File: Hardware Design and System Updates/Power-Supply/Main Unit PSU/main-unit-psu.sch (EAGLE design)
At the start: 15 parts, among them U1 BA033CC0FP-E2TO252-3_ROM, U2 BA033CC0FP-E2TO252-3_ROM

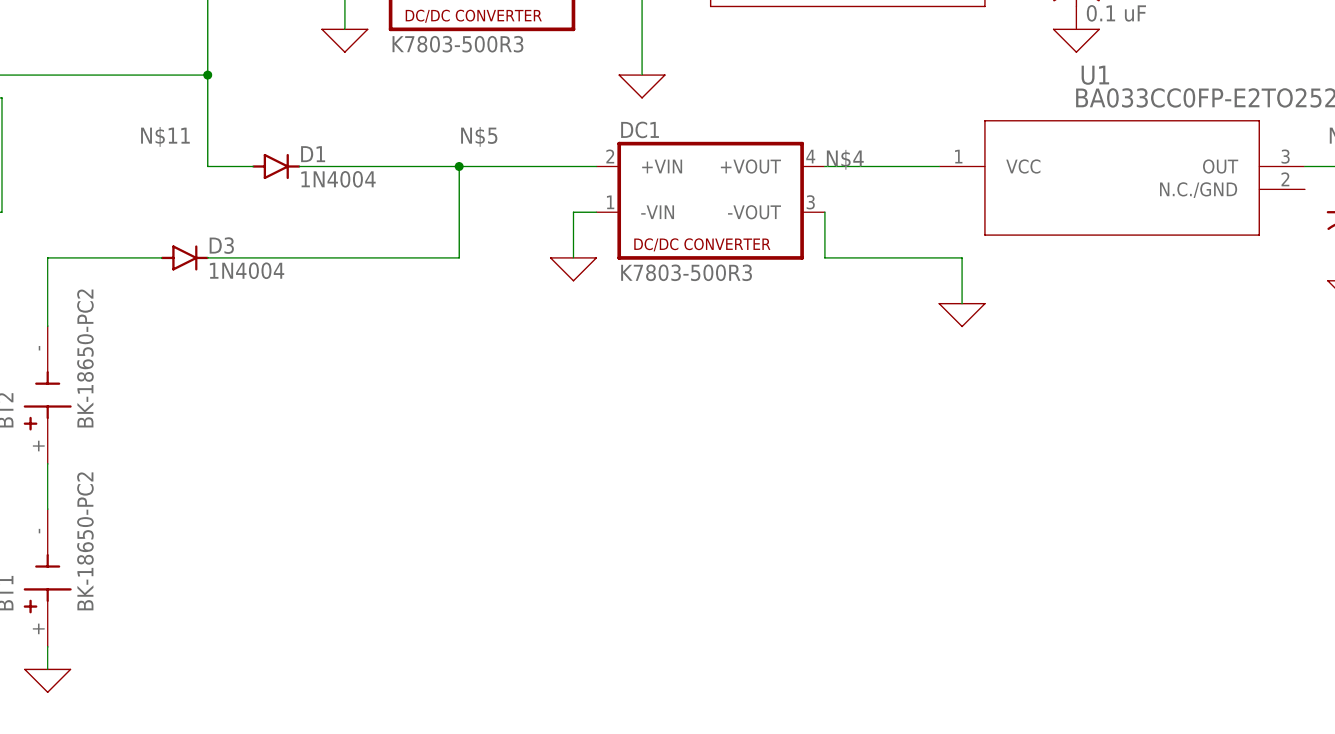
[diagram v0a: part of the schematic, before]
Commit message: Added 5V regulator to PSU schematics
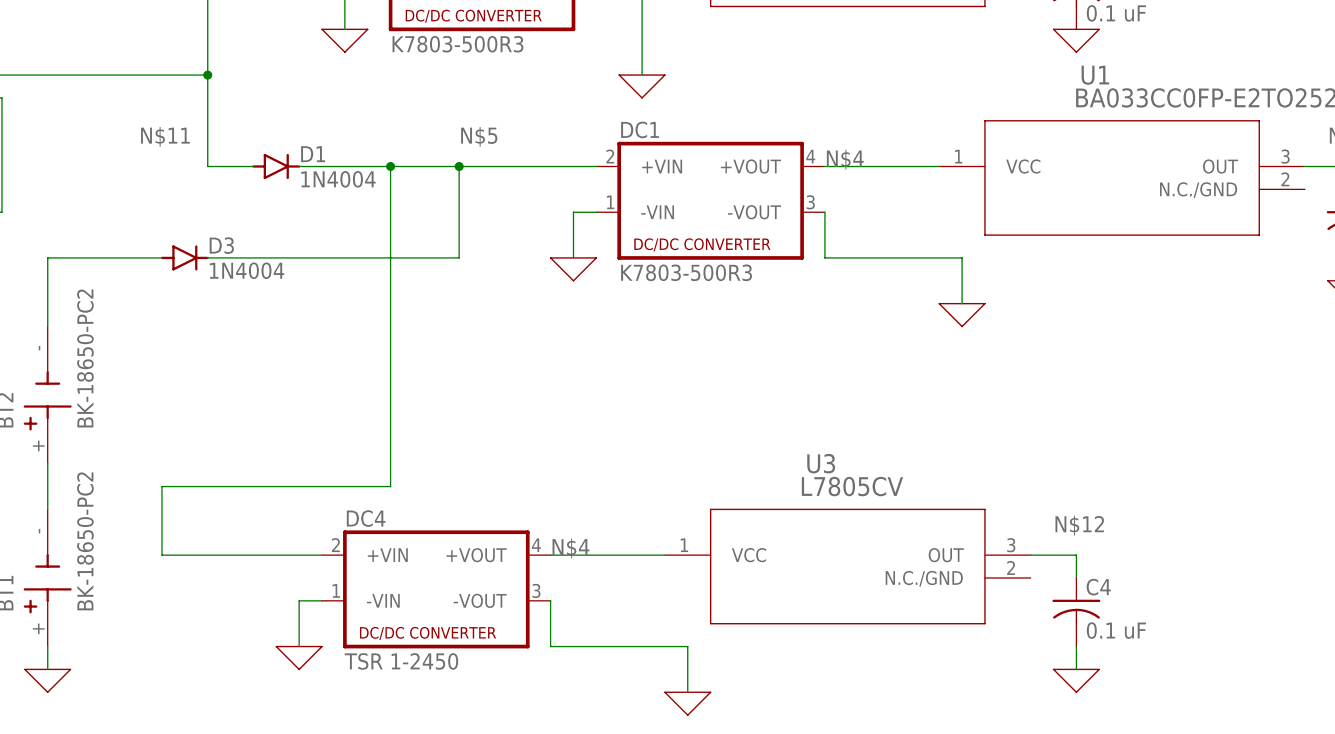
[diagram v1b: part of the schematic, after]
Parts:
- added C4: 0.1 uF, rcl:C-US050-024X044
- added DC4: TSR 1-2450, dc-dc-converter:NME
- added U3: L7805CV, 2023-03-08_12-17-23_Library:BA033CC0FP-E2TO252-3_ROM
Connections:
- net 0: now also C4.2, DC4.-VIN, DC4.-VOUT
- net N$12: now also C4.1, U3.OUT
- net N$4: now also DC4.+VOUT, U3.VCC
- net N$5: now also DC4.+VIN
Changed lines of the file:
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@@
 <layer number="106" name="bPlate" color="4" fill="1" visible="yes" active="yes"/>
 <layer number="107" name="Crop" color="5" fill="1" visible="yes" active="yes"/>
+<layer number="108" name="fp8" color="7" fill="1" visible="no" active="yes"/>
+<layer number="109" name="fp9" color="7" fill="1" visible="no" active="yes"/>
+<layer number="110" name="fp0" color="7" fill="1" visible="no" active="yes"/>
 <layer number="111" name="tGTest" color="7" fill="1" visible="yes" active="yes"/>
 <layer number="112" name="bGTest" color="7" fill="1" visible="yes" active="yes"/>
+<layer number="113" name="ReferenceLS" color="7" fill="1" visible="no" active="no"/>
 <layer number="116" name="Patch_BOT" color="9" fill="4" visible="yes" active="yes"/>
 <layer number="117" name="mPads" color="7" fill="1" visible="yes" active="yes"/>
@@
 <layer number="149" name="mReference" color="7" fill="1" visible="yes" active="yes"/>
 <layer number="150" name="References" color="7" fill="1" visible="yes" active="yes"/>
+<layer number="151" name="HeatSink" color="7" fill="1" visible="no" active="yes"/>
 <layer number="152" name="mbDocu" color="7" fill="1" visible="yes" active="yes"/>
+<layer number="153" name="FabDoc1" color="6" fill="1" visible="no" active="no"/>
+<layer number="154" name="FabDoc2" color="2" fill="1" visible="no" active="no"/>
+<layer number="155" name="FabDoc3" color="7" fill="15" visible="no" active="no"/>
 <layer number="191" name="mNets" color="7" fill="1" visible="yes" active="yes"/>
 <layer number="192" name="mBusses" color="7" fill="1" visible="yes" active="yes"/>
@@
 <layer number="207" name="207bmp" color="8" fill="1" visible="yes" active="yes"/>
 <layer number="208" name="208bmp" color="9" fill="1" visible="yes" active="yes"/>
+<layer number="209" name="209bmp" color="7" fill="1" visible="no" active="yes"/>
+<layer number="210" name="210bmp" color="7" fill="1" visible="no" active="yes"/>
+<layer number="211" name="211bmp" color="7" fill="1" visible="no" active="yes"/>
+<layer number="212" name="212bmp" color="7" fill="1" visible="no" active="yes"/>
+<layer number="213" name="213bmp" color="7" fill="1" visible="no" active="yes"/>
+<layer number="214" name="214bmp" color="7" fill="1" visible="no" active="yes"/>
+<layer number="215" name="215bmp" color="7" fill="1" visible="no" active="yes"/>
 <layer number="216" name="SMD16" color="3" fill="11" visible="yes" active="yes"/>
+<layer number="217" name="217bmp" color="18" fill="1" visible="no" active="no"/>
+<layer number="218" name="218bmp" color="19" fill="1" visible="no" active="no"/>
+<layer number="219" name="219bmp" color="20" fill="1" visible="no" active="no"/>
+<layer number="220" name="220bmp" color="21" fill="1" visible="no" active="no"/>
+<layer number="221" name="221bmp" color="22" fill="1" visible="no" active="no"/>
+<layer number="222" name="222bmp" color="23" fill="1" visible="no" active="no"/>
+<layer number="223" name="223bmp" color="24" fill="1" visible="no" active="no"/>
+<layer number="224" name="224bmp" color="25" fill="1" visible="no" active="no"/>
+<layer number="225" name="225bmp" color="7" fill="1" visible="yes" active="yes"/>
+<layer number="226" name="226bmp" color="7" fill="1" visible="yes" active="yes"/>
+<layer number="227" name="227bmp" color="7" fill="1" visible="yes" active="yes"/>
+<layer number="228" name="228bmp" color="7" fill="1" visible="yes" active="yes"/>
+<layer number="229" name="229bmp" color="7" fill="1" visible="yes" active="yes"/>
+<layer number="230" name="230bmp" color="7" fill="1" visible="yes" active="yes"/>
 <layer number="231" name="Eagle3D_PG1" color="7" fill="1" visible="yes" active="yes"/>
 <layer number="232" name="Eagle3D_PG2" color="7" fill="1" visible="yes" active="yes"/>
 <layer number="233" name="Eagle3D_PG3" color="7" fill="1" visible="yes" active="yes"/>
+<layer number="248" name="Housing" color="7" fill="1" visible="no" active="yes"/>
+<layer number="249" name="Edge" color="7" fill="1" visible="no" active="yes"/>
 <layer number="250" name="Descript" color="3" fill="1" visible="yes" active="yes"/>
 <layer number="251" name="SMDround" color="12" fill="11" visible="yes" active="yes"/>
@@
 <part name="X_10" library="ngspice-simulation" library_urn="urn:adsk.eagle:library:527439" deviceset="GND" device=""/>
 <part name="X_11" library="ngspice-simulation" library_urn="urn:adsk.eagle:library:527439" deviceset="GND" device=""/>
+<part name="DC4" library="dc-dc-converter" library_urn="urn:adsk.eagle:library:208" deviceset="NME" device="" package3d_urn="urn:adsk.eagle:package:12313/1" value="TSR 1-2450"/>
+<part name="X_12" library="ngspice-simulation" library_urn="urn:adsk.eagle:library:527439" deviceset="GND" device=""/>
+<part name="U3" library="2023-03-08_12-17-23_Library" deviceset="BA033CC0FP-E2" device="TO252-3_ROM" value="L7805CV"/>
+<part name="X_13" library="ngspice-simulation" library_urn="urn:adsk.eagle:library:527439" deviceset="GND" device=""/>
+<part name="C4" library="rcl" library_urn="urn:adsk.eagle:library:334" deviceset="C-US" device="050-024X044" package3d_urn="urn:adsk.eagle:package:23643/1" value="0.1 uF"/>
+<part name="X_14" library="ngspice-simulation" library_urn="urn:adsk.eagle:library:527439" deviceset="GND" device=""/>
 </parts>
 <sheets>
@@
 <instance part="X_10" gate="G$1" x="195.58" y="43.18" smashed="yes"/>
 <instance part="X_11" gate="G$1" x="165.1" y="71.12" smashed="yes"/>
+<instance part="DC4" gate="G$1" x="93.98" y="10.16" smashed="yes">
+<attribute name="NAME" x="83.82" y="15.875" size="1.778" layer="95"/>
+<attribute name="VALUE" x="83.82" y="0" size="1.778" layer="96"/>
+</instance>
+<instance part="X_12" gate="G$1" x="78.74" y="2.54" smashed="yes"/>
+<instance part="U3" gate="A" x="116.84" y="12.7" smashed="yes">
+<attribute name="NAME" x="134.9746" y="21.8186" size="2.083" layer="95" ratio="6"/>
+<attribute name="VALUE" x="134.3352" y="19.2786" size="2.083" layer="96" ratio="6"/>
+</instance>
+<instance part="X_13" gate="G$1" x="121.92" y="-2.54" smashed="yes"/>
+<instance part="C4" gate="G$1" x="165.1" y="7.62" smashed="yes">
+<attribute name="NAME" x="166.116" y="8.255" size="1.778" layer="95"/>
+<attribute name="VALUE" x="166.116" y="3.429" size="1.778" layer="96"/>
+</instance>
+<instance part="X_14" gate="G$1" x="165.1" y="0" smashed="yes"/>
 </instances>
 <busses>
@@
 <wire x1="195.58" y1="43.18" x2="195.58" y2="45.72" width="0.1524" layer="91"/>
 </segment>
-</net>
-<net name="N$5" class="0">
-<segment>
-<pinref part="D1" gate="1" pin="C"/>
-<pinref part="DC1" gate="G$1" pin="+VIN"/>
-<wire x1="78.74" y1="55.88" x2="96.52" y2="55.88" width="0.1524" layer="91"/>
-<label x="96.52" y="58.42" size="1.778" layer="95"/>
-<wire x1="96.52" y1="55.88" x2="111.76" y2="55.88" width="0.1524" layer="91"/>
-<wire x1="68.58" y1="45.72" x2="96.52" y2="45.72" width="0.1524" layer="91"/>
-<wire x1="96.52" y1="45.72" x2="96.52" y2="55.88" width="0.1524" layer="91"/>
-<junction x="96.52" y="55.88"/>
-<pinref part="D3" gate="1" pin="C"/>
+<segment>
+<pinref part="X_12" gate="G$1" pin="0"/>
+<pinref part="DC4" gate="G$1" pin="-VIN"/>
+<wire x1="78.74" y1="2.54" x2="78.74" y2="7.62" width="0.1524" layer="91"/>
+<wire x1="78.74" y1="7.62" x2="81.28" y2="7.62" width="0.1524" layer="91"/>
+</segment>
+<segment>
+<pinref part="DC4" gate="G$1" pin="-VOUT"/>
+<wire x1="106.68" y1="7.62" x2="106.68" y2="2.54" width="0.1524" layer="91"/>
+<wire x1="106.68" y1="2.54" x2="121.92" y2="2.54" width="0.1524" layer="91"/>
+<pinref part="X_13" gate="G$1" pin="0"/>
+<wire x1="121.92" y1="-2.54" x2="121.92" y2="2.54" width="0.1524" layer="91"/>
+</segment>
+<segment>
+<pinref part="X_14" gate="G$1" pin="0"/>
+<pinref part="C4" gate="G$1" pin="2"/>
+<wire x1="165.1" y1="0" x2="165.1" y2="2.54" width="0.1524" layer="91"/>
 </segment>
 </net>
@@
 <label x="137.16" y="55.88" size="1.778" layer="95"/>
 <pinref part="U1" gate="A" pin="VCC"/>
+</segment>
+<segment>
+<pinref part="DC4" gate="G$1" pin="+VOUT"/>
+<wire x1="106.68" y1="12.7" x2="119.38" y2="12.7" width="0.1524" layer="91"/>
+<label x="106.68" y="12.7" size="1.778" layer="95"/>
+<pinref part="U3" gate="A" pin="VCC"/>
 </segment>
 </net>
@@
 <junction x="195.58" y="55.88"/>
 </segment>
+<segment>
+<wire x1="160.02" y1="12.7" x2="165.1" y2="12.7" width="0.1524" layer="91"/>
+<label x="162.56" y="15.24" size="1.778" layer="95"/>
+<pinref part="U3" gate="A" pin="OUT"/>
+<pinref part="C4" gate="G$1" pin="1"/>
+<wire x1="165.1" y1="10.16" x2="165.1" y2="12.7" width="0.1524" layer="91"/>
+</segment>
 </net>
 <net name="N$6" class="0">
@@
 </segment>
 </net>
+<net name="N$5" class="0">
+<segment>
+<pinref part="DC4" gate="G$1" pin="+VIN"/>
+<wire x1="63.5" y1="12.7" x2="81.28" y2="12.7" width="0.1524" layer="91"/>
+<wire x1="63.5" y1="12.7" x2="63.5" y2="20.32" width="0.1524" layer="91"/>
+<wire x1="63.5" y1="20.32" x2="88.9" y2="20.32" width="0.1524" layer="91"/>
+<pinref part="D1" gate="1" pin="C"/>
+<pinref part="DC1" gate="G$1" pin="+VIN"/>
+<wire x1="78.74" y1="55.88" x2="88.9" y2="55.88" width="0.1524" layer="91"/>
+<label x="96.52" y="58.42" size="1.778" layer="95"/>
+<wire x1="88.9" y1="55.88" x2="96.52" y2="55.88" width="0.1524" layer="91"/>
+<wire x1="96.52" y1="55.88" x2="111.76" y2="55.88" width="0.1524" layer="91"/>
+<wire x1="68.58" y1="45.72" x2="96.52" y2="45.72" width="0.1524" layer="91"/>
+<wire x1="96.52" y1="45.72" x2="96.52" y2="55.88" width="0.1524" layer="91"/>
+<junction x="96.52" y="55.88"/>
+<pinref part="D3" gate="1" pin="C"/>
+<wire x1="88.9" y1="20.32" x2="88.9" y2="55.88" width="0.1524" layer="91"/>
+<junction x="88.9" y="55.88"/>
+</segment>
+</net>
